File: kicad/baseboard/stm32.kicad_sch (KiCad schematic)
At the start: 17 parts, among them J1 Conn_01x06_Pin, J10 Conn_01x06_Pin, J12 Conn_01x06_Pin, J4 Conn_01x06_Pin, J7 Conn_01x06_Pin, U4 YAAJ_BlackPill, U7 DRV8871DDA, U8 AMS1117-3.3

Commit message: Baseboard partial routing
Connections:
- net BatterieSwitch: now reaches C4.2, C5.2, U7.5 (VM)
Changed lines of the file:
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@@
+		)
+	)
+	(global_label "BatterieSwitch"
+		(shape input)
+		(at 68.58 44.45 180)
+		(fields_autoplaced yes)
+		(effects
+			(font
+				(size 1.016 1.016)
+			)
+			(justify right)
+		)
+		(property "Intersheetrefs" "${INTERSHEET_REFS}"
+			(at 55.2784 44.45 0)
+			(effects
+				(font
+					(size 1.27 1.27)
+				)
+				(justify right)
+				(hide yes)
+			)
 		)
 	)

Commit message: Finish PCB routing
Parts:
- D3: footprint LED_SMD:LED_0603_1608Metric -> LED_SMD:LED_0805_2012Metric
- D4: footprint LED_SMD:LED_0603_1608Metric -> LED_SMD:LED_0805_2012Metric; LCSC Part # (none) -> C2296; Part Description Green 572nm LED Indication - Discrete 2.2V 2-SMD, No Lead -> Yellow LED; j C2297 -> (none)
- U8: footprint Package_TO_SOT_SMD:SOT-223 -> PCM_SparkFun-Semiconductor-Standard:SOT-223-3_TabPin2
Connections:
- net BAT AD IN is gone; now on net BatterieSwitch: R9.2
- net MOTOR INT A: now also J7.4 (Pin_4)
- net MOTOR INT B: now also J7.3 (Pin_3)
- net MOTOR PWM 1: no longer J7.4 (Pin_4)
- net MOTOR PWM 2: no longer J7.3 (Pin_3)
- net +5V renamed +5v
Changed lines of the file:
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@@
+	)
+	(junction
+		(at 88.9 96.52)
+		(diameter 0)
+		(color 0 0 0 0)
 	)
 	(junction
@@
 	)
 	(junction
-		(at 88.9 96.52)
-		(diameter 0)
-		(color 0 0 0 0)
-	)
-	(junction
 		(at 88.9 104.14)
 		(diameter 0)
@@
 	(wire
 		(pts
+			(xy 142.24 17.78) (xy 148.59 17.78)
+		)
+		(stroke
+			(width 0)
+			(type default)
+		)
+	)
+	(wire
+		(pts
 			(xy 162.56 91.44) (xy 167.64 91.44)
 		)
@@
 	(wire
 		(pts
+			(xy 88.9 96.52) (xy 105.41 96.52)
+		)
+		(stroke
+			(width 0)
+			(type default)
+		)
+	)
+	(wire
+		(pts
 			(xy 39.37 101.6) (xy 55.88 101.6)
 		)
@@
 		(pts
 			(xy 115.57 86.36) (xy 121.92 86.36)
-		)
-		(stroke
-			(width 0)
-			(type default)
-		)
-	)
-	(wire
-		(pts
-			(xy 88.9 96.52) (xy 97.79 96.52)
 		)
 		(stroke
@@
 		)
 	)
-	(label "BAT AD IN"
-		(at 203.2 69.85 180)
-		(effects
-			(font
-				(size 1.27 1.27)
-			)
-			(justify right bottom)
-		)
-	)
-	(label "MOTOR PWM 2"
-		(at 91.44 50.8 0)
-		(effects
-			(font
-				(size 1.27 1.27)
-			)
-			(justify left bottom)
-		)
-	)
 	(label "MOTOR INT B"
 		(at 167.64 104.14 0)
@@
 		)
 	)
+	(label "MOTOR INT B"
+		(at 93.98 50.8 0)
+		(effects
+			(font
+				(size 1.27 1.27)
+			)
+			(justify left bottom)
+		)
+	)
 	(label "CS1"
 		(at 170.18 81.28 0)
@@
 	)
 	(label "MOTOR INT A"
+		(at 93.98 48.26 0)
+		(effects
+			(font
+				(size 1.27 1.27)
+			)
+			(justify left bottom)
+		)
+	)
+	(label "MOTOR INT A"
 		(at 167.64 106.68 0)
 		(effects
@@
 			)
 			(justify right bottom)
-		)
-	)
-	(label "MOTOR PWM 1"
-		(at 91.44 48.26 0)
-		(effects
-			(font
-				(size 1.27 1.27)
-			)
-			(justify left bottom)
 		)
 	)
@@
 				)
 				(justify right)
+				(hide yes)
+			)
+		)
+	)
+	(global_label "+5v"
+		(shape input)
+		(at 105.41 96.52 0)
+		(fields_autoplaced yes)
+		(effects
+			(font
+				(size 1.27 1.27)
+			)
+			(justify left)
+		)
+		(property "Intersheetrefs" "${INTERSHEET_REFS}"
+			(at 112.2398 96.52 0)
+			(effects
+				(font
+					(size 1.27 1.27)
+				)
+				(justify left)
+				(hide yes)
+			)
+		)
+	)
+	(global_label "BatterieSwitch"
+		(shape input)
+		(at 203.2 69.85 180)
+		(fields_autoplaced yes)
+		(effects
+			(font
+				(size 1.016 1.016)
+			)
+			(justify right)
+		)
+		(property "Intersheetrefs" "${INTERSHEET_REFS}"
+			(at 189.8984 69.85 0)
+			(effects
+				(font
+					(size 1.27 1.27)
+				)
+				(justify right)
+				(hide yes)
+			)
+		)
+	)
+	(global_label "+5v"
+		(shape input)
+		(at 148.59 17.78 0)
+		(fields_autoplaced yes)
+		(effects
+			(font
+				(size 1.27 1.27)
+			)
+			(justify left)
+		)
+		(property "Intersheetrefs" "${INTERSHEET_REFS}"
+			(at 155.4198 17.78 0)
+			(effects
+				(font
+					(size 1.27 1.27)
+				)
+				(justify left)
 				(hide yes)
 			)
@@
 			)
 		)
-		(property "Footprint" "LED_SMD:LED_0603_1608Metric"
+		(property "Footprint" "LED_SMD:LED_0805_2012Metric"
 			(at 196.85 99.06 0)
 			(effects
@@
 				(path "/e63e39d7-6ac0-4ffd-8aa3-1841a4541b55/f8d89121-d537-41fd-ae3a-d2339816f145"
 					(reference "D3")
-					(unit 1)
-				)
-			)
-		)
-	)
-	(symbol
-		(lib_id "power:+5V")
-		(at 97.79 96.52 270)
-		(unit 1)
-		(exclude_from_sim no)
-		(in_bom yes)
-		(on_board yes)
-		(dnp no)
-		(fields_autoplaced yes)
-		(property "Reference" "#PWR020"
-			(at 93.98 96.52 0)
-			(effects
-				(font
-					(size 1.27 1.27)
-				)
-				(hide yes)
-			)
-		)
-		(property "Value" "+5V"
-			(at 101.6 96.5199 90)
-			(effects
-				(font
-					(size 1.27 1.27)
-				)
-				(justify left)
-			)
-		)
-		(property "Footprint" ""
-			(at 97.79 96.52 0)
-			(effects
-				(font
-					(size 1.27 1.27)
-				)
-				(hide yes)
-			)
-		)
-		(property "Datasheet" ""
-			(at 97.79 96.52 0)
-			(effects
-				(font
-					(size 1.27 1.27)
-				)
-				(hide yes)
-			)
-		)
-		(property "Description" "Power symbol creates a global label with name \"+5V\""
-			(at 97.79 96.52 0)
-			(effects
-				(font
-					(size 1.27 1.27)
-				)
-				(hide yes)
-			)
-		)
-		(pin "1"
-		)
-		(instances
-			(project ""
-				(path "/e63e39d7-6ac0-4ffd-8aa3-1841a4541b55/f8d89121-d537-41fd-ae3a-d2339816f145"
-					(reference "#PWR020")
 					(unit 1)
 				)
@@
 			)
 		)
-		(property "Footprint" "Package_TO_SOT_SMD:SOT-223"
+		(property "Footprint" "PCM_SparkFun-Semiconductor-Standard:SOT-223-3_TabPin2"
 			(at 139.7 35.56 0)
 			(effects
@@
 			)
 		)
-		(property "Footprint" "LED_SMD:LED_0603_1608Metric"
+		(property "Footprint" "LED_SMD:LED_0805_2012Metric"
 			(at 196.85 101.6 0)
 			(effects
@@
 			)
 		)
-		(property "Part Description" "	Green 572nm LED Indication - Discrete 2.2V 2-SMD, No Lead"
+		(property "Part Description" "Yellow LED"
 			(at 196.85 101.6 0)
 			(effects
@@
 			)
 		)
-		(property "j" "C2297"
+		(property "LCSC Part #" "C2296"
 			(at 196.85 101.6 90)
 			(effects
@@
 					(unit 1)
 				)
-			)
-		)
-	)
-	(symbol
-		(lib_id "power:+5V")
-		(at 142.24 17.78 0)
-		(unit 1)
-		(exclude_from_sim no)
-		(in_bom yes)
-		(on_board yes)
-		(dnp no)
-		(property "Reference" "#PWR017"
-			(at 142.24 21.59 0)
-			(effects
-				(font
-					(size 1.27 1.27)
-				)
-				(hide yes)
-			)
-		)
-		(property "Value" "+5V"
-			(at 144.272 14.224 0)
-			(effects
-				(font
-					(size 1.27 1.27)
-				)
-			)
-		)
-		(property "Footprint" ""
-			(at 142.24 17.78 0)
-			(effects
-				(font
-					(size 1.27 1.27)
-				)
-				(hide yes)
-			)
-		)
-		(property "Datasheet" ""
-			(at 142.24 17.78 0)
-			(effects
-				(font
-					(size 1.27 1.27)
-				)
-				(hide yes)
-			)
-		)
-		(property "Description" "Power symbol creates a global label with name \"+5V\""
-			(at 142.24 17.78 0)
-			(effects
-				(font
-					(size 1.27 1.27)
-				)
-				(hide yes)
-			)
-		)
-		(pin "1"
-		)
-		(instances
-			(project ""
-				(path "/e63e39d7-6ac0-4ffd-8aa3-1841a4541b55/f8d89121-d537-41fd-ae3a-d2339816f145"
-					(reference "#PWR017")
-					(unit 1)
-				)

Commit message: Setup baseboard pcb production settings
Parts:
- J1, J10, J12, J4, J7: LCSC Part # (none) -> C160255
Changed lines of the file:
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@@
+			)
+		)
+		(property "LCSC Part #" "C160255"
+			(at 83.82 101.6 0)
+			(effects
+				(font
+					(size 1.27 1.27)
+				)
+				(hide yes)
 			)
 		)
@@
 			)
 		)
+		(property "LCSC Part #" "C160255"
+			(at 111.76 50.8 0)
+			(effects
+				(font
+					(size 1.27 1.27)
+				)
+				(hide yes)
+			)
+		)
 		(pin "3"
 		)
@@
 			)
 		)
+		(property "LCSC Part #" "C160255"
+			(at 50.8 101.6 0)
+			(effects
+				(font
+					(size 1.27 1.27)
+				)
+				(hide yes)
+			)
+		)
 		(pin "1"
 		)
@@
 			)
 		)
+		(property "LCSC Part #" "C160255"
+			(at 34.29 101.6 0)
+			(effects
+				(font
+					(size 1.27 1.27)
+				)
+				(hide yes)
+			)
+		)
 		(pin "1"
 		)
@@
 			(at 67.31 101.6 0)
 			(effects
+				(font
+					(size 1.27 1.27)
+				)
+				(hide yes)
+			)
+		)
+		(property "LCSC Part #" "C160255"
+			(at 67.31 101.6 0)
+			(effects

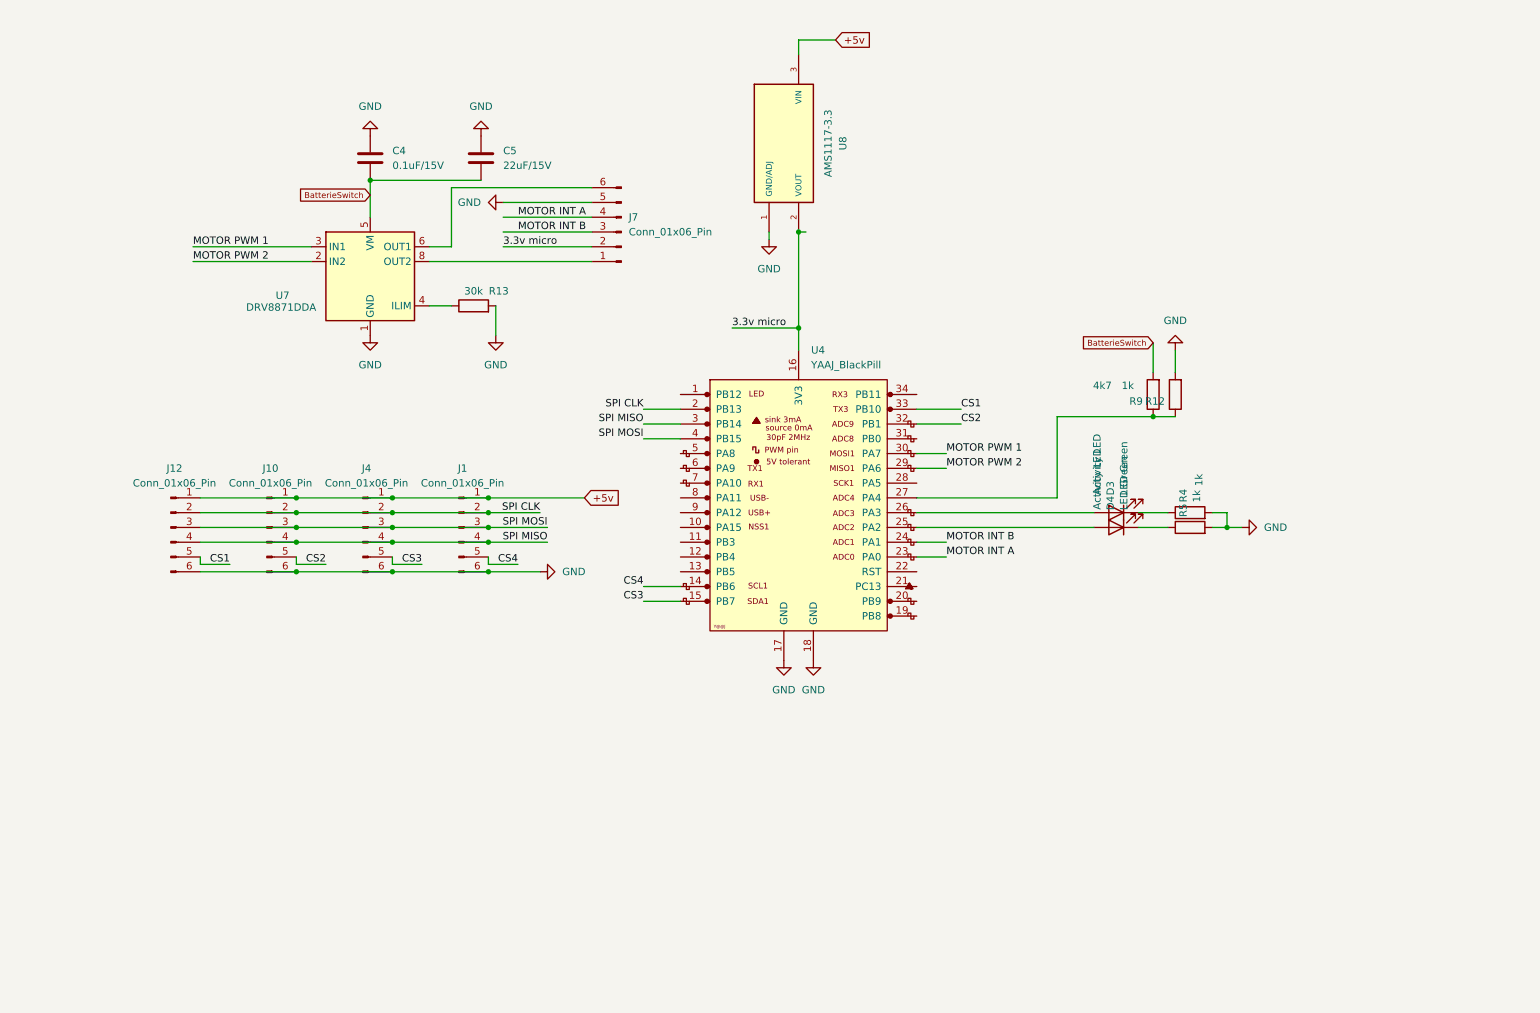
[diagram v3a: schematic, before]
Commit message: Correct V1 mistakes : Turned MISO, Correct STM32 template.   Add BMO055 Gyroskope . Add servo connector. Add serial port connector. Add Pi - Stm32 serial connection. Add Silkscreen texts.
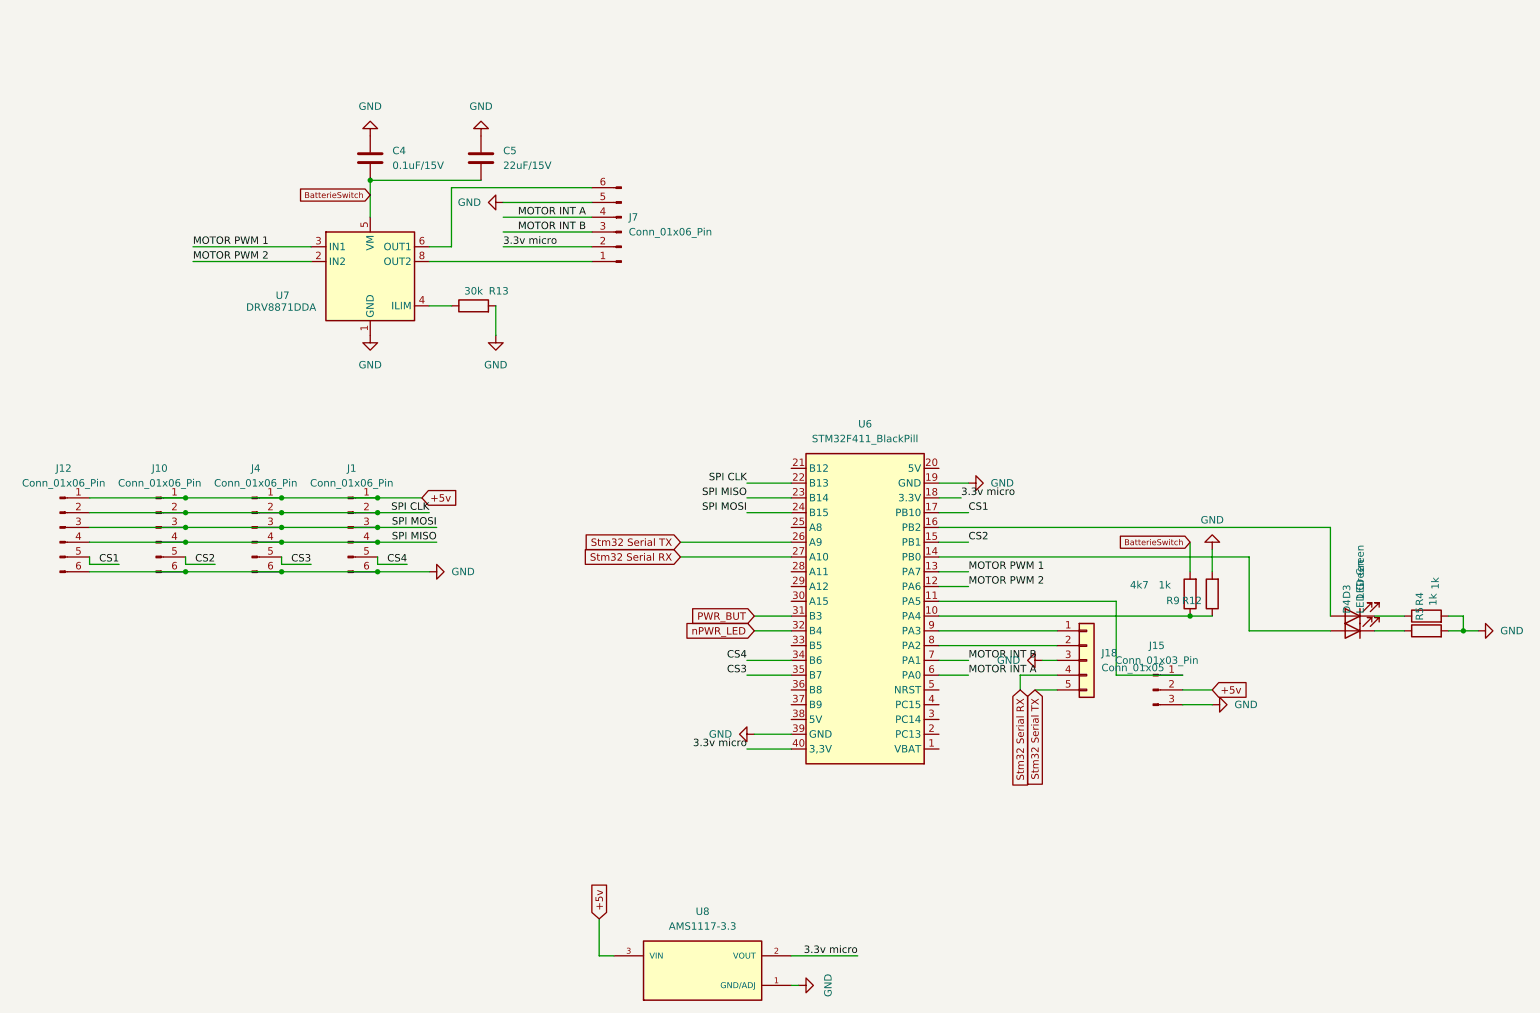
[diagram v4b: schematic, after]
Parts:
- removed U4: YAAJ_BlackPill, Library:YAAJ_BlackPill_2, symbol New_Library:YAAJ_BlackPill
- added J15: Conn_01x03_Pin, Connector_JST:JST_XH_B3B-XH-A_1x03_P2.50mm_Vertical, symbol Connector:Conn_01x03_Pin
- added J18: Conn_01x05, Connector_JST:JST_XH_B5B-XH-AM_1x05_P2.50mm_Vertical, symbol Connector_Generic:Conn_01x05
- added U6: STM32F411_BlackPill, Package_DIP:DIP-40_W15.24mm_Socket, symbol STM32F411_BlackPill:STM32F411_BlackPill
- J1, J10, J12, J4, J7: footprint Connector_JST:JST_EH_B6B-EH-A_1x06_P2.50mm_Vertical -> Connector_JST:JST_XH_B6B-XH-A_1x06_P2.50mm_Vertical
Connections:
- net +5v: now also J15.2 (Pin_2)
- net 3.3v micro: now also U6.18 (3.3V), U6.40 (3,3V)
- net CS1: now also U6.17 (PB10)
- net CS2: now also U6.15 (PB1)
- net CS3: now also U6.35 (B7)
- net CS4: now also U6.34 (B6)
- net GND: now also J15.3 (Pin_3), J18.3 (Pin_3), U6.19 (GND), U6.39 (GND)
- net MOTOR INT A: now also U6.6 (PA0)
- net MOTOR INT B: now also U6.7 (PA1)
- net MOTOR PWM 1: now also U6.13 (PA7)
- net MOTOR PWM 2: now also U6.12 (PA6)
- net SPI CLK: now also U6.22 (B13)
- net SPI MISO: now also U6.23 (B14)
- net SPI MOSI: now also U6.24 (B15)
- net at D3.2 (A): now also U6.16 (PB2)
- net at D4.2 (A): now also U6.14 (PB0)
- net at R12.1, R9.1: now also U6.10 (PA4)
- new net: J15.1 (Pin_1), U6.11 (PA5)
- new net: J18.2 (Pin_2), U6.8 (PA2)
- new net: J18.1 (Pin_1), U6.9 (PA3)
- new net PWR_BUT: U6.31 (B3)
- new net Stm32 Serial RX: J18.4 (Pin_4), U6.27 (A10)
- new net Stm32 Serial TX: J18.5 (Pin_5), U6.26 (A9)
- new net nPWR_LED: U6.32 (B4)
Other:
- note removed: "Activity LED"
- moved on the sheet: D3, D4, J1, J10, J12, J4, R12, R4, R5, R9, U8
